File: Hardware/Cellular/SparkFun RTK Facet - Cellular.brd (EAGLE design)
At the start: 60 x 30.7 mm, 69 parts, among them IC1 SN74AVC4T774PW, J18 SARA_USB, J2 NANO_SIM, J3 U.FL, J6 DIAG, Q2 310mA/60V/1.6Ω, Q3 310mA/60V/1.6Ω, Q4 310mA/60V/1.6Ω, Q5 20V/0.2A/8MHz/1.2Ω/1Vth, Q7 310mA/60V/1.6Ω, U1 SARA-R510M8S, U8 74HC1G04

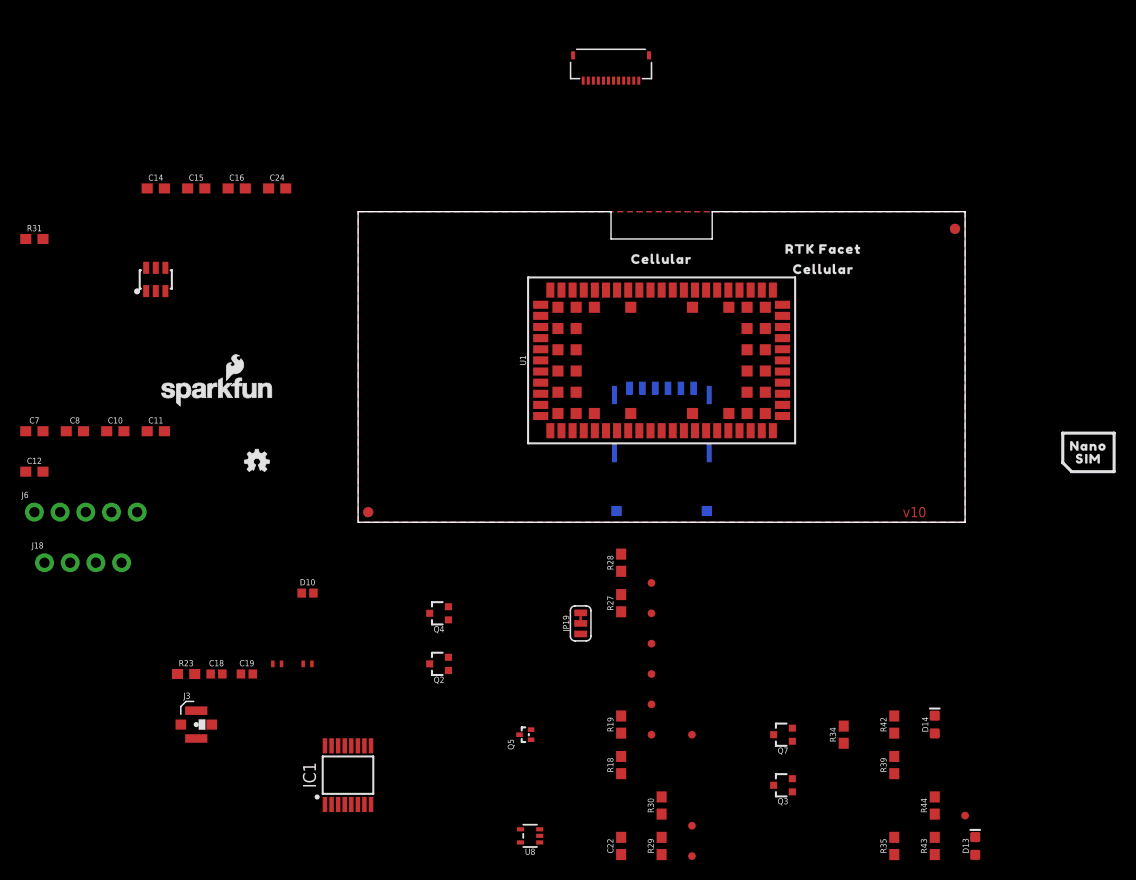
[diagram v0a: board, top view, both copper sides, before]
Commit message: Paul edits. Move dummy to sub-folder
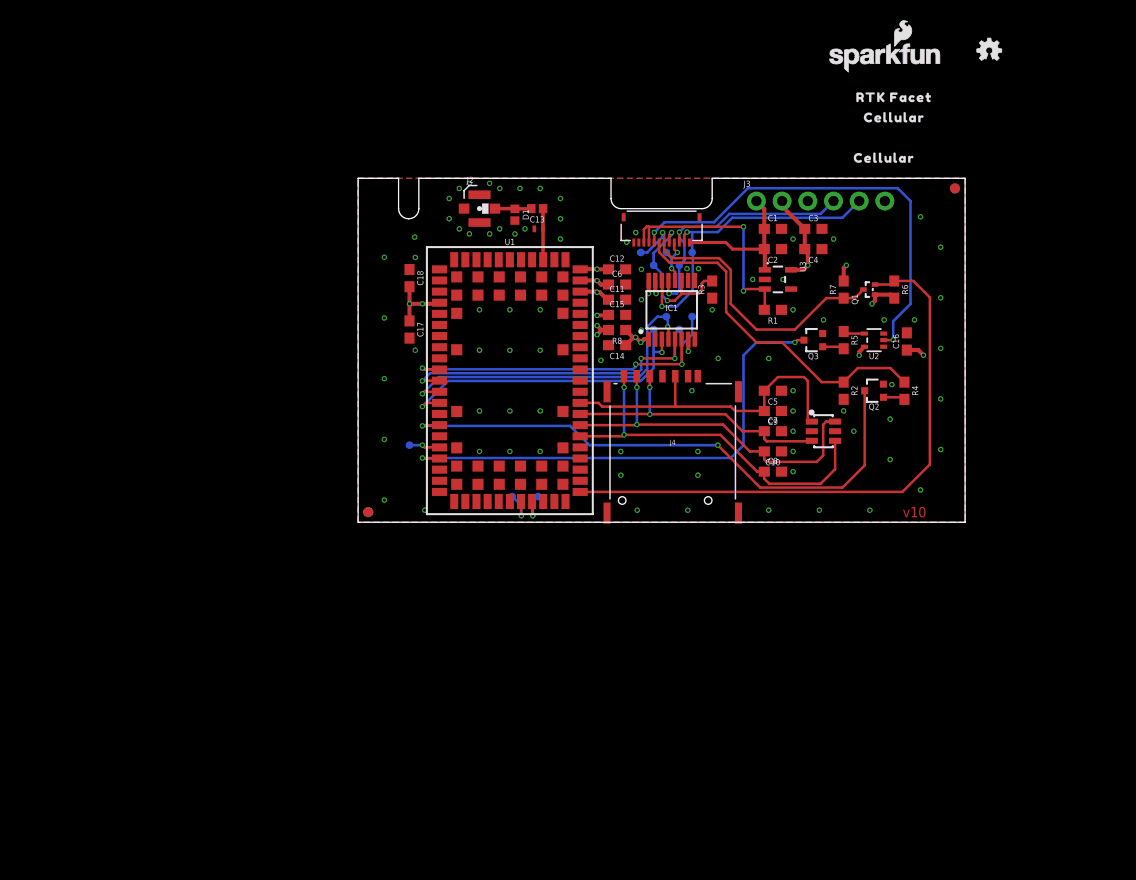
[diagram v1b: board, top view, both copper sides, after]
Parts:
- removed C19: 27pF, New_Parts:0402
- removed C22: 0.1uF, SparkFun-Capacitors:0603
- removed C24: 15pF, SparkFun-Capacitors:0603
- removed D10: PESD0402, New_Parts:0402
- removed D13: BLUE, SparkFun-LED:LED-0603
- removed D14: WHITE, SparkFun-LED:LED-0603
- removed D8: DT1042-04SO-7, ublox:SOT23-6L
- removed FRAME1: FRAME-LETTER, SparkFun-Aesthetics:CREATIVE_COMMONS
- removed FRAME2: FRAME-LETTERNO_PACKAGE, SparkFun-Aesthetics:DUMMY
- removed J18: SARA_USB, SparkFun-Connectors:1X04_NO_SILK
- removed J6: DIAG, SparkFun-Connectors:1X05_NO_SILK
- removed JP19: JUMPER-SMT_3_1-NC_TRACE_SILK, SparkFun-Jumpers:SMT-JUMPER_3_1-NC_TRACE_SILK
- removed L2: 68nH, New_Parts:0402_COILCRAFT
- removed Q4, Q7: 310mA/60V/1.6Ω, SparkFun-DiscreteSemi:SOT323
- removed Q5: 20V/0.2A/8MHz/1.2Ω/1Vth, SparkFun-DiscreteSemi:SOT-416FL
- removed R18, R19, R39, R44: 100k, SparkFun-Resistors:0603
- removed R23: 10k, SparkFun-Resistors:0603
- removed R27, R28, R34, R42, R43: 1k, SparkFun-Resistors:0603
- removed R29, R30: 2.2k, SparkFun-Resistors:0603
- removed R31: 0, SparkFun-Resistors:0603
- removed R35: 470, SparkFun-Resistors:0603
- removed TP13: TEST-POINT3, SparkFun-Connectors:PAD.03X.03
- removed U8: 74HC1G04, SparkFun-IC-Logic:SOT353
- added C1, C17, C3: 1.0uF, SparkFun-Capacitors:0603
- added C13: 33pF, New_Parts:0402
- added C2, C4, C5, C6: 0.1uF, SparkFun-Capacitors:0603
- added C9: 47pF, SparkFun-Capacitors:0603
- added D1: PESD0402, New_Parts:0402
- added D2: DT1042-04SO-7, ublox:SOT23-6L
- added FRAME3: FRAME-LEDGER, SparkFun-Aesthetics:CREATIVE_COMMONS
- added J4: (no value), SparkFun-Connectors:NANO_SIM_PP
- added LOGO1: SPECIAL_INSTRUCTIONS-ORDERING, SparkFun-Aesthetics:ORDERING_INSTRUCTIONS
- added Q1: 20V/0.2A/8MHz/1.2Ω/1Vth, SparkFun-DiscreteSemi:SOT-416FL
- added R1, R2, R3: 100k, SparkFun-Resistors:0603
- added R4, R5: 1k, SparkFun-Resistors:0603@1
- added R6, R7: 2.2k, SparkFun-Resistors:0603@1
- added R8: 0, SparkFun-Resistors:0603@1
- added TP10, TP11, TP9: TEST-POINT3, SparkFun-Connectors:PAD.03X.03
- added U2: 74HC1G04, SparkFun-IC-Logic:SOT353
- added U3: AP2112K-3.3, SparkFun-IC-Power:SOT23-5
- C11: value 47pF -> 68pF
- C12: value 0.1uF -> 10uF
- C15: value 68pF -> 15pF
- C16: value 10uF -> 0.1uF
- C18: value 33pF -> 0.1uF; device New_Parts:0402 -> SparkFun-Capacitors:0603
- J2: value NANO_SIM -> U.FL; device ublox:NANO_SIM_WURTH_693043020611 -> SparkFun-Connectors:U.FL
- J3: value U.FL -> DIAG; device SparkFun-Connectors:U.FL -> SparkFun-Connectors:1X06_NO_SILK
- moved LOGO3 83.0 mm to (62.4, 46.6)
- moved J3 75.8 mm to (39.4, 31.8)
- moved LOGO5 73.8 mm to (52.1, 45.9)
- moved C7 73.0 mm to (41.0, 9.00)
- moved C8 69.1 mm to (41.0, 5.00)
- moved C16 67.9 mm to (54.2, 17.9), turned to 90 degrees
- moved C10 65.0 mm to (41.0, 7.00), turned to 180 degrees
- moved C12 61.0 mm to (25.6, 25.0)
- moved TP7 59.7 mm to (30.5, 26.7), flipped to the bottom
- moved IC1 56.0 mm to (31.0, 21.0)
- moved TP8 55.5 mm to (29.2, 25.4), flipped to the bottom
- moved Q2 50.8 mm to (51.0, 13.0)
- moved L1 50.2 mm to (17.9, 29.0), turned to 180 degrees
- moved C14 48.2 mm to (25.6, 17.5), turned to 180 degrees
- moved TP12 47.9 mm to (27.9, 26.7), flipped to the bottom
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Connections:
- removed net 1.8V: J6.4
- removed net LTE_NI: Q3.3, R35.1, R39.1
- removed net N$16: C19.1, D10.1, L2.P$1, R23.2
- removed net N$35: Q3.1, R34.2
- removed net N$37: D13.C, R35.2
- removed net N$43: JP19.2, Q5.2, R29.1
- removed net N$47: Q7.1, R42.2
- removed net N$49: D14.C, R43.2
- removed net SARA_!ON!: Q7.3, R43.1, R44.1, TP13.P$1
- removed net SARA_ANT_DET: R23.1, U1.62
- removed net SARA_GPIO3: JP19.1
- removed net SARA_NI: R34.1, U1.16
- removed net SARA_TP: U1.19
- removed net SARA_USB_D+: J18.2, U1.29
- removed net SARA_USB_D-: J18.1, U1.28
- removed net SARA_VUSB_DET: J18.3, U1.17
- removed net VIN: J6.1
- new net MAIN_3V3: J1.10, J1.9, R1.2, U3.3
- new net N$1: TP9.1, U1.28
- new net N$2: TP10.1, U1.29
- new net N$3: TP11.1, U1.17
- net 3.3V: now also C11.1, C12.1, C3.1, C4.2, C6.1, J3.2, R7.2, U2.5, U3.5; no longer C14.1, C24.1, D13.A, D14.A, J1.3, J1.4, J6.2, R30.2, R39.2, R44.2, U8.5
- net GND: now also C1.2, C11.2, C12.2, C17.2, C18.1, C2.1, C3.2, C4.1, C5.1, C6.2, C9.1, D1.2, D2.2, D2.5, J1.11, J1.12, J2.1, J2.2, J3.6, J4.C5, R1.1, R2.2, R3.1, U1.9, U2.3, U3.2; no longer C11.1, C12.1, C19.2, C22.2, C24.2, D10.2, D8.2, D8.5, J1.1, J1.2, J18.4, J2.C5, J3.1, J3.2, J6.5, Q4.2, Q7.2, R18.2, R19.1, U8.3
- net LTE_!RESET!: now also J1.8, U2.2; no longer J1.5, U8.2
- net LTE_CTSI: now also J1.5, R3.2, TP8.1; no longer J1.8, R19.2, TP8.P$1
- net LTE_INT: now also J1.6, Q1.3, R7.1, TP12.1; no longer J1.7, Q5.3, R30.1, TP12.P$1
- net LTE_PWR_ON: now also J1.7, R2.1, R4.1; no longer J1.6, R18.1, R27.1
- net LTE_RTSO: now also J1.4, TP7.1; no longer J1.9, TP7.P$1
- net LTE_RXI: now also J1.3, J3.4, TP6.1; no longer J1.10, TP6.P$1
- net LTE_TXO: now also J1.2, J3.5, TP5.1; no longer J1.11, TP5.P$1
- net N$15: now also C13.2, D1.1, J2.FEED; no longer C18.2, J3.FEED, L2.P$2
- net N$26: now also R4.2; no longer R27.2
- net N$27: now also Q3.1, R5.2; no longer Q4.1, R28.2
- net N$28: now also R5.1, U2.4; no longer R28.1, U8.4
- net N$31: now also C17.1, C18.2, R8.2; no longer R31.2
- net SARA_!RESET!: now also Q3.3; no longer Q4.3
- net SARA_ANT: now also C13.1; no longer C18.1
- net SARA_CTSO: now also TP3.1; no longer TP3.P$1
- net SARA_EXT_INT: now also Q1.2, R6.1; no longer JP19.3
- net SARA_RTSI: now also TP4.1; no longer TP4.P$1
- net SARA_RXO: now also TP1.1; no longer TP1.P$1
- net SARA_TXI: now also TP2.1; no longer TP2.P$1
- net SIM_CLK: now also D2.4, J4.C3; no longer D8.1, J2.C3
- net SIM_IO: now also D2.6, J4.C7; no longer D8.6, J2.C7
- net SIM_RST: now also D2.3, J4.C2; no longer D8.4, J2.C2
- net VCCIO: now also C14.1, J3.3, Q1.1, R6.2, R8.1; no longer C22.1, J6.3, Q5.1, R29.2, R31.1, R42.1
- net VOUT: now also C1.1, C2.2, J1.1, J3.1, U3.1; no longer J1.12
- net VSIM: now also C5.2, C9.2, D2.1, J4.C1; no longer C11.2, C12.2, D8.3, J2.C1
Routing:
- net SARA_EXT_INT: track 0.00 -> 58.4 mm
- net SARA_PWR_ON: track 0.00 -> 56.3 mm, vias 0 -> 2
- net VCCIO: track 0.00 -> 54.4 mm, vias 0 -> 5
- net SARA_!RESET!: track 0.00 -> 49.5 mm, vias 0 -> 2
- net LTE_!RESET!: track 0.00 -> 44.1 mm, vias 0 -> 2
- net SIM_CLK: track 0.00 -> 36.9 mm, vias 0 -> 2
- net SIM_IO: track 0.00 -> 35.4 mm, vias 0 -> 2
- net SARA_RTSI: track 0.00 -> 35.4 mm, vias 0 -> 3
- net LTE_PWR_ON: track 0.00 -> 34.0 mm
- net SARA_TXI: track 0.00 -> 33.8 mm, vias 0 -> 2
- net SARA_CTSO: track 0.00 -> 33.2 mm, vias 0 -> 3
- net VSIM: track 0.00 -> 33.0 mm
- net SARA_RXO: track 0.00 -> 32.3 mm, vias 0 -> 2
- net LTE_INT: track 0.00 -> 31.6 mm, vias 0 -> 1
- net LTE_TXO: track 0.00 -> 31.5 mm, vias 0 -> 2
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- added copper zone on layer 15, net 3.3V
- added copper zone on layer 2, net GND
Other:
- board size 60 x 30.7 mm -> 60 x 34 mm
- board text added: "JLCPCB JLC7628 Impedance Control 4-Layer PCB 1.6mm Thickness 1oz Copper (Outer Layers) HASL RoHS Finish"
- board text added: "Paul Clark"

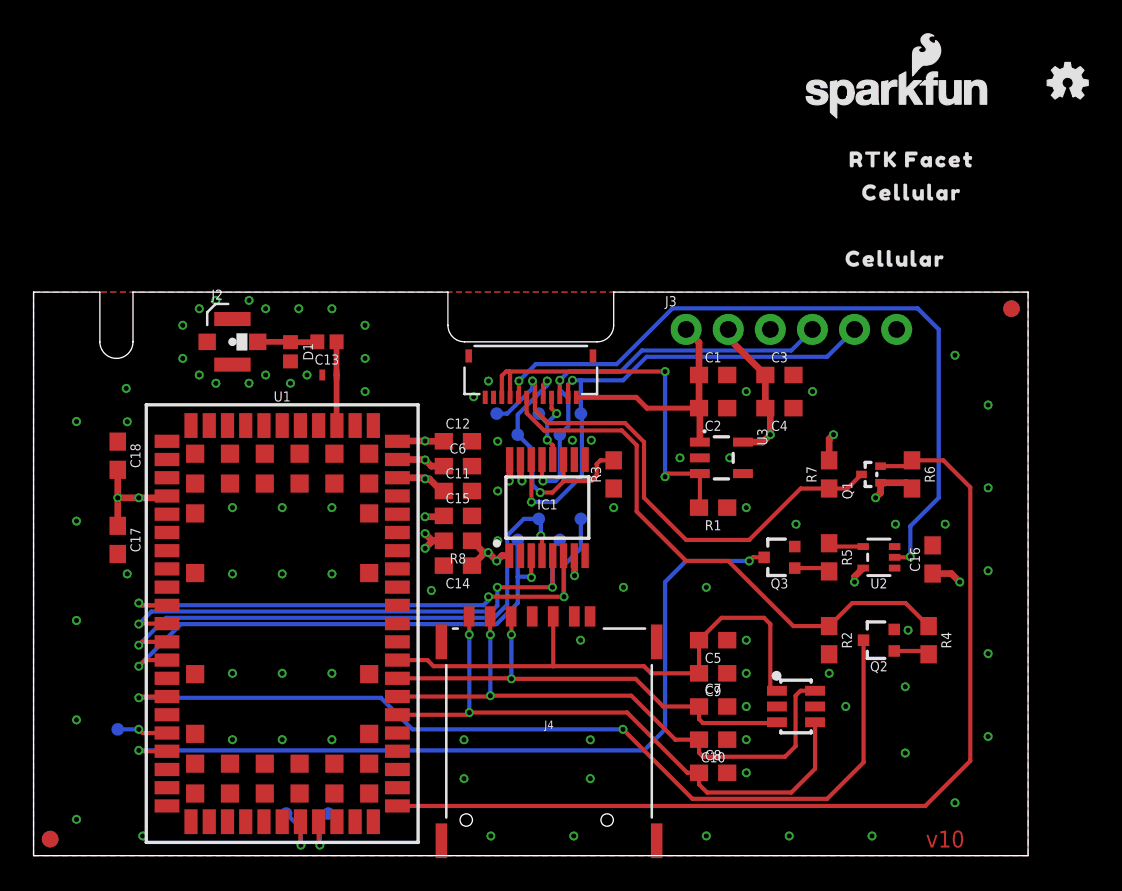
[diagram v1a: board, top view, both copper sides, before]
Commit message: Add Buzzard text
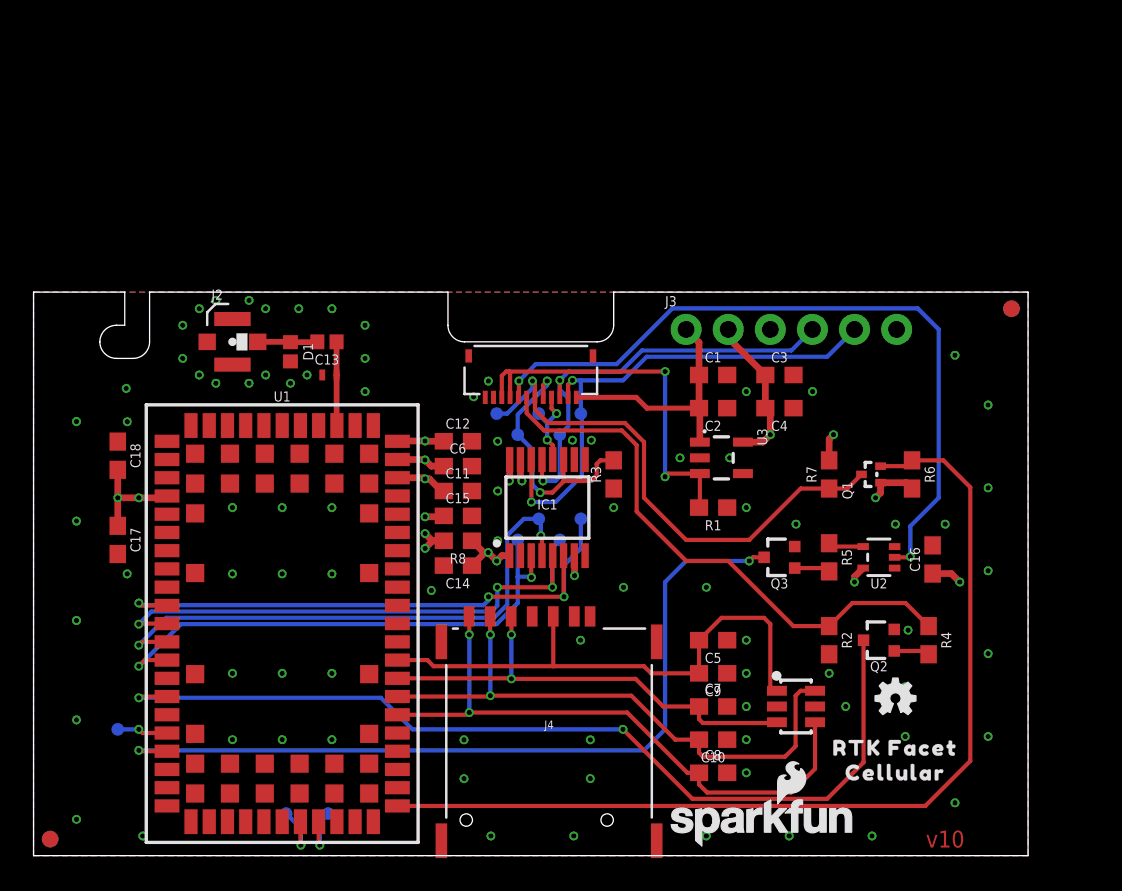
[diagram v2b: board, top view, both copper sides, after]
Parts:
- removed U$13: (no value), output:CELLULAR0
- added LOGO2: SFE_LOGO_NAME_FLAME.1_INCH, SparkFun-Aesthetics:SFE_LOGO_NAME_FLAME_.1
- added LOGO4: OSHW-LOGOMINI, SparkFun-Aesthetics:OSHW-LOGO-MINI
- added U$1: (no value), output:RTK_FACET0
- added U$3: (no value), output:CELLULAR1
- added U$4: (no value), output:#VOUT#0
- added U$5: (no value), output:#3#3V#0
- added U$6: (no value), output:#VCCIO#0
- added U$7: (no value), output:#LTE_RXI#0
- added U$8: (no value), output:#LTE_TXO#0
- added U$9: (no value), output:#GND#0
- moved LOGO5 44.7 mm to (44.0, 2.00)
- moved LOGO3 38.6 mm to (52.0, 9.50)
- moved U$14 35.5 mm to (52.0, 6.50)
- moved U$2 35.0 mm to (52.0, 5.00)
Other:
- outline, holes or cut-outs redrawn
- board text added: "Dimensions in mm"

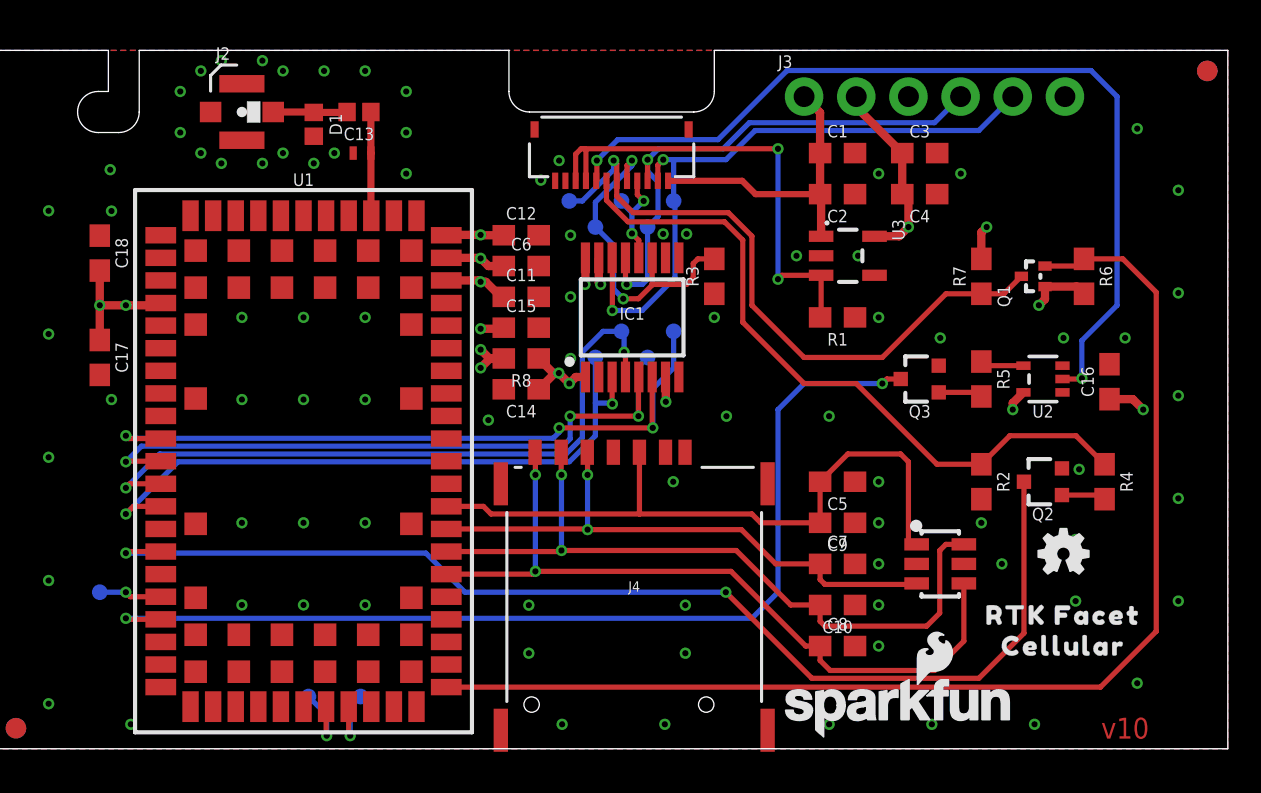
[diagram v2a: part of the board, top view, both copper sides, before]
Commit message: Add cellular board production files
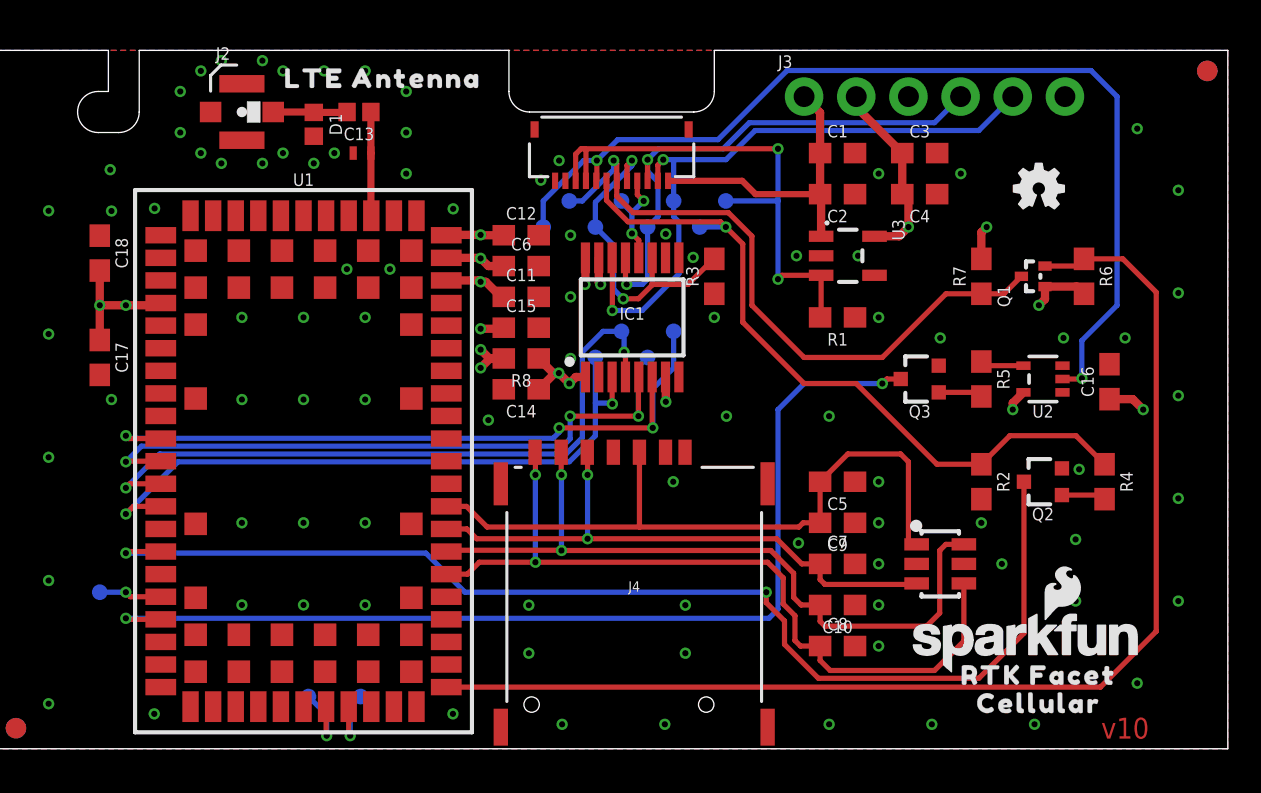
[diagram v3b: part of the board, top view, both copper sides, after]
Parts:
- added TP13, TP14, TP15: TEST-POINT3, SparkFun-Connectors:PAD.03X.03
- added U$10: (no value), output:LTE_ANTENNA0
- added U$15: (no value), output:RTK5#SVG0
- J4: device SparkFun-Connectors:NANO_SIM_PP -> SparkFun-Connectors:NANO_SIM_PP_REDUCED_PADS
- R4, R5, R6, R7, R8: device SparkFun-Resistors:0603@1 -> SparkFun-Resistors:0603
- moved U$3 40.0 mm to (14.5, 19.0)
- moved U$1 39.9 mm to (14.5, 20.2)
- moved LOGO2 37.9 mm to (15.2, 21.9)
- moved LOGO4 37.7 mm to (14.5, 5.69)
- moved LOGO3 17.8 mm to (50.8, 27.3)
- moved LOGO5 6.99 mm to (50.2, 5.17)
- moved U$14 3.16 mm to (50.8, 3.58)
- moved U$2 3.04 mm to (50.8, 2.21)
- moved U$130 1.27 mm to (29.2, 3.62)
- moved U$131 1.27 mm to (30.6, 3.62)
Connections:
- net LTE_!RESET!: now also TP14.1
- net LTE_PWR_ON: now also TP13.1
- net MAIN_3V3: now also TP15.1
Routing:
- net LTE_!RESET!: track 44.1 -> 48.8 mm
- net MAIN_3V3: track 23.4 -> 26.0 mm
- net SIM_CLK: track 36.9 -> 38.2 mm
- net LTE_PWR_ON: track 34.0 -> 35.2 mm, vias 0 -> 1
- net SARA_PWR_ON: track 56.3 -> 57.2 mm
- net VSIM: track 33.0 -> 33.8 mm
- net SIM_IO: track 35.4 -> 36.1 mm
